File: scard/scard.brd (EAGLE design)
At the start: 90 x 90 mm, 72 parts, among them Q1 FDN360P, X1 COAX, X2 1365-20

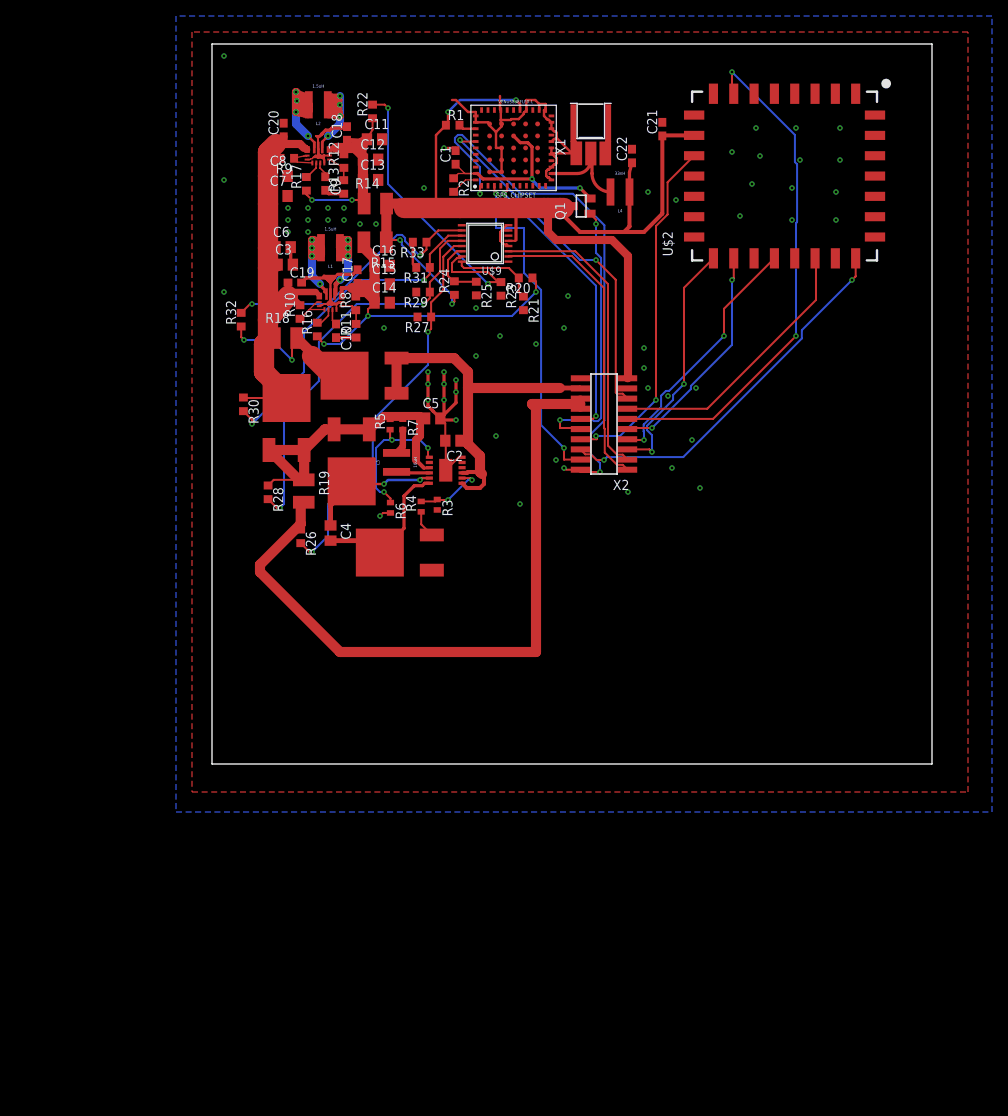
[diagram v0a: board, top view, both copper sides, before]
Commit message: shrunk size to save money
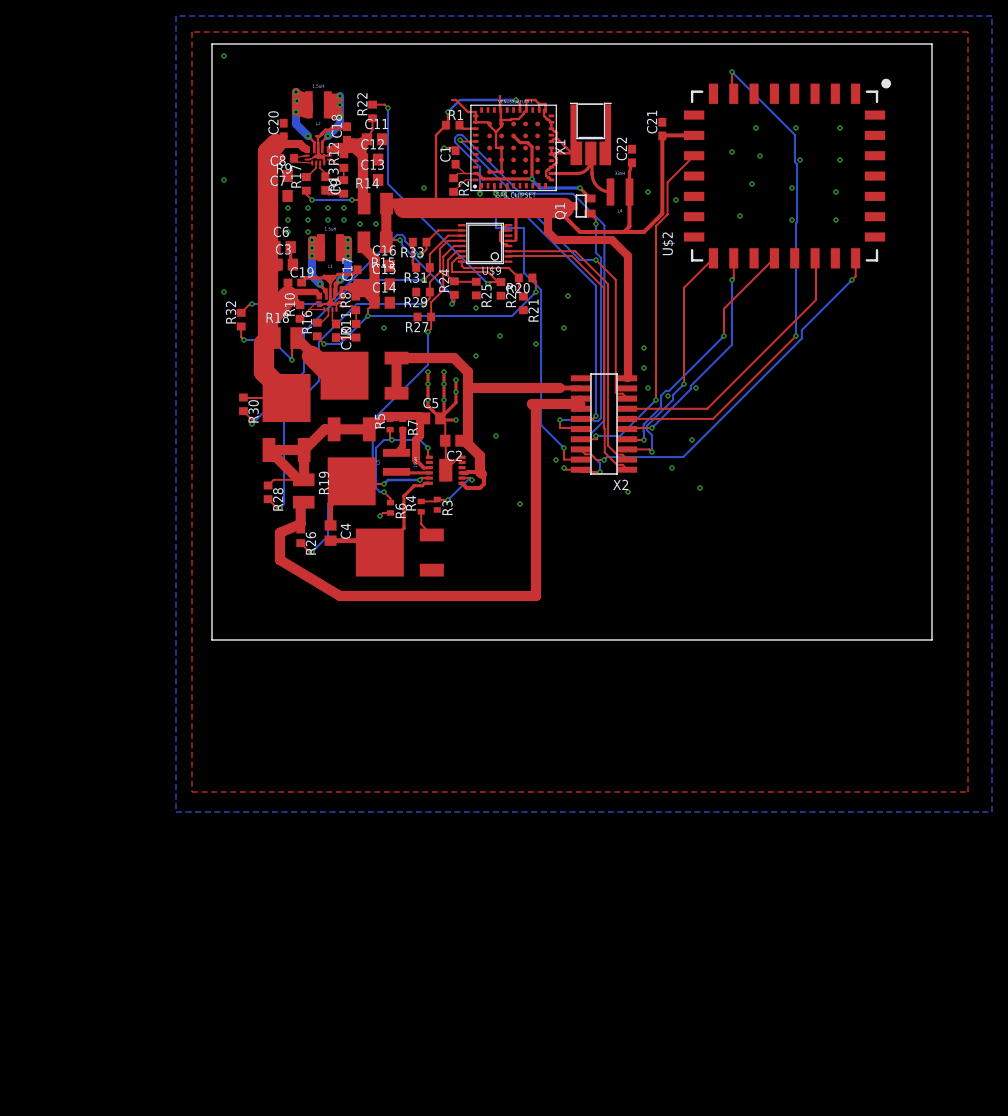
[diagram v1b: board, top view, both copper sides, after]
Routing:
- net VBATT: track 88.8 -> 74.6 mm
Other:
- board size 90 x 90 mm -> 90 x 74.5 mm
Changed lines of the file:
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@@
 <grid distance="0.5" unitdist="mm" unit="mm" style="lines" multiple="1" display="no" altdistance="5" altunitdist="mil" altunit="mil"/>
 <layers>
-<layer number="1" name="Top" color="4" fill="1" visible="no" active="yes"/>
+<layer number="1" name="Top" color="4" fill="1" visible="yes" active="yes"/>
 <layer number="2" name="Route2" color="1" fill="3" visible="no" active="no"/>
 <layer number="3" name="Route3" color="4" fill="3" visible="no" active="no"/>
@@
 <layer number="14" name="Route14" color="1" fill="6" visible="no" active="no"/>
 <layer number="15" name="Route15" color="4" fill="6" visible="no" active="no"/>
-<layer number="16" name="Bottom" color="1" fill="1" visible="no" active="yes"/>
-<layer number="17" name="Pads" color="2" fill="1" visible="no" active="yes"/>
+<layer number="16" name="Bottom" color="1" fill="1" visible="yes" active="yes"/>
+<layer number="17" name="Pads" color="2" fill="1" visible="yes" active="yes"/>
 <layer number="18" name="Vias" color="2" fill="1" visible="yes" active="yes"/>
-<layer number="19" name="Unrouted" color="6" fill="1" visible="no" active="yes"/>
-<layer number="20" name="Dimension" color="15" fill="1" visible="no" active="yes"/>
-<layer number="21" name="tPlace" color="7" fill="1" visible="no" active="yes"/>
-<layer number="22" name="bPlace" color="7" fill="1" visible="no" active="yes"/>
-<layer number="23" name="tOrigins" color="15" fill="1" visible="no" active="yes"/>
-<layer number="24" name="bOrigins" color="15" fill="1" visible="no" active="yes"/>
-<layer number="25" name="tNames" color="7" fill="1" visible="no" active="yes"/>
-<layer number="26" name="bNames" color="7" fill="1" visible="no" active="yes"/>
-<layer number="27" name="tValues" color="7" fill="1" visible="no" active="yes"/>
-<layer number="28" name="bValues" color="7" fill="1" visible="no" active="yes"/>
+<layer number="19" name="Unrouted" color="6" fill="1" visible="yes" active="yes"/>
+<layer number="20" name="Dimension" color="15" fill="1" visible="yes" active="yes"/>
+<layer number="21" name="tPlace" color="7" fill="1" visible="yes" active="yes"/>
+<layer number="22" name="bPlace" color="7" fill="1" visible="yes" active="yes"/>
+<layer number="23" name="tOrigins" color="15" fill="1" visible="yes" active="yes"/>
+<layer number="24" name="bOrigins" color="15" fill="1" visible="yes" active="yes"/>
+<layer number="25" name="tNames" color="7" fill="1" visible="yes" active="yes"/>
+<layer number="26" name="bNames" color="7" fill="1" visible="yes" active="yes"/>
+<layer number="27" name="tValues" color="7" fill="1" visible="yes" active="yes"/>
+<layer number="28" name="bValues" color="7" fill="1" visible="yes" active="yes"/>
 <layer number="29" name="tStop" color="7" fill="3" visible="no" active="yes"/>
 <layer number="30" name="bStop" color="7" fill="6" visible="no" active="yes"/>
@@
 <layer number="37" name="tTest" color="7" fill="1" visible="no" active="yes"/>
 <layer number="38" name="bTest" color="7" fill="1" visible="no" active="yes"/>
-<layer number="39" name="tKeepout" color="4" fill="11" visible="no" active="yes"/>
-<layer number="40" name="bKeepout" color="1" fill="11" visible="no" active="yes"/>
-<layer number="41" name="tRestrict" color="4" fill="10" visible="no" active="yes"/>
-<layer number="42" name="bRestrict" color="1" fill="10" visible="no" active="yes"/>
+<layer number="39" name="tKeepout" color="4" fill="11" visible="yes" active="yes"/>
+<layer number="40" name="bKeepout" color="1" fill="11" visible="yes" active="yes"/>
+<layer number="41" name="tRestrict" color="4" fill="10" visible="yes" active="yes"/>
+<layer number="42" name="bRestrict" color="1" fill="10" visible="yes" active="yes"/>
 <layer number="43" name="vRestrict" color="2" fill="10" visible="no" active="yes"/>
 <layer number="44" name="Drills" color="7" fill="1" visible="no" active="yes"/>
-<layer number="45" name="Holes" color="7" fill="1" visible="no" active="yes"/>
+<layer number="45" name="Holes" color="7" fill="1" visible="yes" active="yes"/>
 <layer number="46" name="Milling" color="3" fill="1" visible="no" active="yes"/>
 <layer number="47" name="Measures" color="7" fill="1" visible="no" active="yes"/>
@@
 <layer number="49" name="Reference" color="7" fill="1" visible="no" active="yes"/>
 <layer number="50" name="dxf" color="7" fill="1" visible="no" active="no"/>
-<layer number="51" name="tDocu" color="7" fill="1" visible="no" active="yes"/>
-<layer number="52" name="bDocu" color="7" fill="1" visible="no" active="yes"/>
+<layer number="51" name="tDocu" color="7" fill="1" visible="yes" active="yes"/>
+<layer number="52" name="bDocu" color="7" fill="1" visible="yes" active="yes"/>
 <layer number="53" name="tGND_GNDA" color="7" fill="9" visible="no" active="no"/>
 <layer number="54" name="bGND_GNDA" color="1" fill="9" visible="no" active="no"/>
@@
 <board>
 <plain>
-<wire x1="0" y1="0" x2="90" y2="0" width="0" layer="20"/>
-<wire x1="90" y1="0" x2="90" y2="90" width="0" layer="20"/>
+<wire x1="0" y1="15.5" x2="90" y2="15.5" width="0" layer="20"/>
+<wire x1="90" y1="15.5" x2="90" y2="90" width="0" layer="20"/>
 <wire x1="90" y1="90" x2="0" y2="90" width="0" layer="20"/>
-<wire x1="0" y1="90" x2="0" y2="0" width="0" layer="20"/>
+<wire x1="0" y1="90" x2="0" y2="15.5" width="0" layer="20"/>
 </plain>
 <attributes>
@@
 </class>
 </classes>
-<designrules name="oshpark-2layer">
+<designrules name="oshpark-2layer *">
 <description language="de">&lt;b&gt;EAGLE Design Rules&lt;/b&gt;
 &lt;p&gt;
@@
 <param name="mlMinCreamFrame" value="0mil"/>
 <param name="mlMaxCreamFrame" value="0mil"/>
-<param name="mlViaStopLimit" value="0mil"/>
+<param name="mlViaStopLimit" value="10mm"/>
 <param name="srRoundness" value="0"/>
 <param name="srMinRoundness" value="0mil"/>
@@
 <wire x1="46.05" y1="45" x2="46.05" y2="44.405" width="0.8128" layer="1"/>
 <wire x1="40" y1="45" x2="40.5" y2="44.5" width="1.27" layer="1"/>
-<wire x1="40.5" y1="44.5" x2="40.5" y2="14" width="1.27" layer="1"/>
-<wire x1="40.5" y1="14" x2="16" y2="14" width="1.27" layer="1"/>
-<wire x1="16" y1="14" x2="6" y2="24" width="1.27" layer="1"/>
-<wire x1="6" y1="24" x2="6" y2="24.91" width="1.27" layer="1"/>
-<wire x1="6" y1="24.91" x2="11.09" y2="30" width="1.27" layer="1"/>
+<wire x1="40.5" y1="44.5" x2="40.5" y2="21" width="1.27" layer="1"/>
+<wire x1="40.5" y1="21" x2="16" y2="21" width="1.27" layer="1"/>
+<wire x1="16" y1="21" x2="8.5" y2="25.5" width="1.27" layer="1"/>
+<wire x1="8.5" y1="25.5" x2="8.5" y2="28.91" width="1.27" layer="1"/>
+<wire x1="8.5" y1="28.91" x2="11.09" y2="30" width="1.27" layer="1"/>
 <wire x1="46.05" y1="45" x2="40" y2="45" width="1.27" layer="1"/>
 <wire x1="11.09" y1="30" x2="11.09" y2="32" width="1.27" layer="1"/>

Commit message: changes from design review
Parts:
- removed R20, R21, R22, R23, R24, R25, R27, R29, R31, R33: 1k, resistor:R0603
- removed R26, R28: 4k, resistor:R0603
- removed R30, R32: 5k, resistor:R0603
- removed U$3: B085BM30, calsat:TO-252
- removed U$9: ADC128D818, adc:ADC12_SD
- added A1, A3: INA3221-Q1, calsat:VQFN16
- added C23, C24: 0.1uF, resistor:C0603
- added D1: ES2D, diode:SMB
- added PAD1, PAD2, PAD3, PAD4, PAD5: (no value), wirepad:SMD2,54-5,08
- moved C21 74.3 mm to (8.29, 22.6), flipped to the bottom, turned to 270 degrees
- moved U$2 65.6 mm to (23.6, 28.9), flipped to the bottom, turned to 270 degrees
- moved X2 46.7 mm to (15.5, 10.0), turned to 0 degrees
- moved C22 15.4 mm to (43.5, 63.5), turned to 0 degrees
- moved X1 11.8 mm to (35.9, 85.0)
- moved L4 11.1 mm to (40.5, 75.0)
- moved GPS_CHIPSET 8.57 mm to (32.5, 70.2), turned to 270 degrees
- moved Q1 7.78 mm to (40.3, 64.7), turned to 180 degrees
- moved C1 6.80 mm to (24.9, 71.8)
- moved R2 6.80 mm to (24.7, 68.4)
- moved L3 4.03 mm to (22.6, 33.7)
- moved L1 3.54 mm to (14.3, 61.0)
- moved C10 3.54 mm to (15.0, 50.6)
- moved C11 3.54 mm to (19.8, 74.6)
- moved C12 3.54 mm to (19.3, 72.0)
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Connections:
- removed net N$16: R20.2, R21.1, U$9.16
- removed net N$17: R22.2, R23.1, U$9.15
- removed net N$18: R24.2, R25.1, U$9.14
- removed net N$19: R26.2, R27.1, U$9.13
- removed net N$2: CHRG_IC.10, L3.1
- removed net N$20: R28.2, R29.1, U$9.12
- removed net N$21: R30.2, R31.1, U$9.11
- removed net N$23: R32.2, R33.1, U$9.10
- new net N$32: A3.15
- new net N$33: A3.14
- new net N$34: A3.2
- new net N$35: A3.1
- net +12V: now also PAD4.1, PAD5.1; no longer X2.18
- net +3V3: now also A1.11, A1.14, A1.4, A3.4, C23.1, C24.1, PAD3.1; no longer R24.1, U$9.5, X2.19
- net GND: now also A1.17, A1.3, A3.17, A3.3, A3.5, C23.2, C24.2, PAD1.1, PAD2.1, X2.19; no longer R21.2, R23.2, R25.2, R27.2, R29.2, R31.2, R33.2, U$9.4, U$9.7, U$9.8
- net I2C_SCL: now also A1.6, A3.6; no longer U$9.3
- net I2C_SDA: now also A1.5, A1.7, A3.7; no longer U$9.2
- net N$3: now also D1.C; no longer U$3.1
- net N$4: now also L3.1
- net N$6: now also CHRG_IC.10
- net REG0_3V3: now also A1.12; no longer R20.1
- net REG1_3V3: now also A1.15; no longer R22.1
- net SYS_UNREG: now also A3.11; no longer R30.1
- net SYS_UNREG_CUR: now also A3.12; no longer R32.1
- net VBATT: now also A1.1, X2.18; no longer R26.1
- net VBATT_CUR: now also A1.2, D1.A; no longer R28.1, U$3.2, U$3.3
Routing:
- net TARE_GPIO: track 64.6 -> 12.2 mm, vias 2 -> 1
- net GPS_EN: track 35.1 -> 86.0 mm, vias 2 -> 4
- net N$20: track 50.7 -> 0.00 mm, vias 2 -> 0
- net P1PPS: track 35.8 -> 85.6 mm, vias 2 -> 4
- net N$19: track 48.4 -> 0.00 mm, vias 2 -> 0
- net I2C_SDA: track 38.0 -> 81.6 mm, vias 0 -> 3
- net STS: track 44.6 -> 87.9 mm
- net N$21: track 42.4 -> 0.00 mm, vias 2 -> 0
- net N$17: track 40.3 -> 0.00 mm, vias 2 -> 0
- net UART0_TXD: track 42.0 -> 80.0 mm, vias 2 -> 4
- net I2C_SCL: track 37.5 -> 75.0 mm, vias 0 -> 3
- net N$23: track 34.8 -> 0.00 mm, vias 2 -> 0
- net VBATT_CUR: track 45.8 -> 75.9 mm, vias 0 -> 2
- net IMU_EN: track 44.3 -> 21.9 mm, vias 2 -> 1
- net REG1_3V3: track 31.4 -> 52.2 mm, vias 2 -> 3
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- added copper zone on layer 1, net NONE
- added copper zone on layer 16, net NONE
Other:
- board size 90 x 74.5 mm -> 47 x 86.5 mm

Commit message: fixed ground plane on GPS
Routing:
- net GND: track 153.2 -> 159.1 mm, vias 59 -> 60
- added copper zone on layer 1, net NONE2
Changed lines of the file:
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@@
 <wire x1="38.0125" y1="82.61" x2="38.0959" y2="82.61" width="0.4064" layer="1"/>
 <wire x1="33.6875" y1="82.61" x2="33.6041" y2="82.61" width="0.4064" layer="1"/>
+<wire x1="32.49" y1="74.93" x2="33.29" y2="74.93" width="0.1524" layer="1"/>
+<wire x1="31.69" y1="74.93" x2="32.49" y2="74.93" width="0.1524" layer="1"/>
+<wire x1="37.69625" y1="74.6848" x2="37.8748" y2="74.50625" width="0.3048" layer="1"/>
+<wire x1="37.8748" y1="72.6252" x2="38.5" y2="72" width="0.3048" layer="1"/>
+<wire x1="37.8748" y1="74.50625" x2="37.8748" y2="72.6252" width="0.3048" layer="1"/>
+<wire x1="36.49" y1="74.93" x2="36.7352" y2="74.6848" width="0.3048" layer="1"/>
+<wire x1="36.7352" y1="74.6848" x2="37.69625" y2="74.6848" width="0.3048" layer="1"/>
+<via x="38.5" y="72" extent="1-16" drill="0.35"/>
 </signal>
 <signal name="STS">
@@
 </polygon>
 </signal>
+<signal name="NONE2">
+<polygon width="0.1524" layer="1" pour="cutout">
+<vertex x="27.5" y="75"/>
+<vertex x="37" y="75"/>
+<vertex x="37" y="65.5"/>
+<vertex x="27.5" y="65.5"/>
+</polygon>
+</signal>
